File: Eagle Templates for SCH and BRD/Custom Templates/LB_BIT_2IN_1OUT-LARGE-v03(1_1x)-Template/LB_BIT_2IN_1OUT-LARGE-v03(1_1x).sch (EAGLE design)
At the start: 22 parts, among them U1 LV321SOT23-5, U2 LV321SOT23-5, U6 LV321SOT23-5

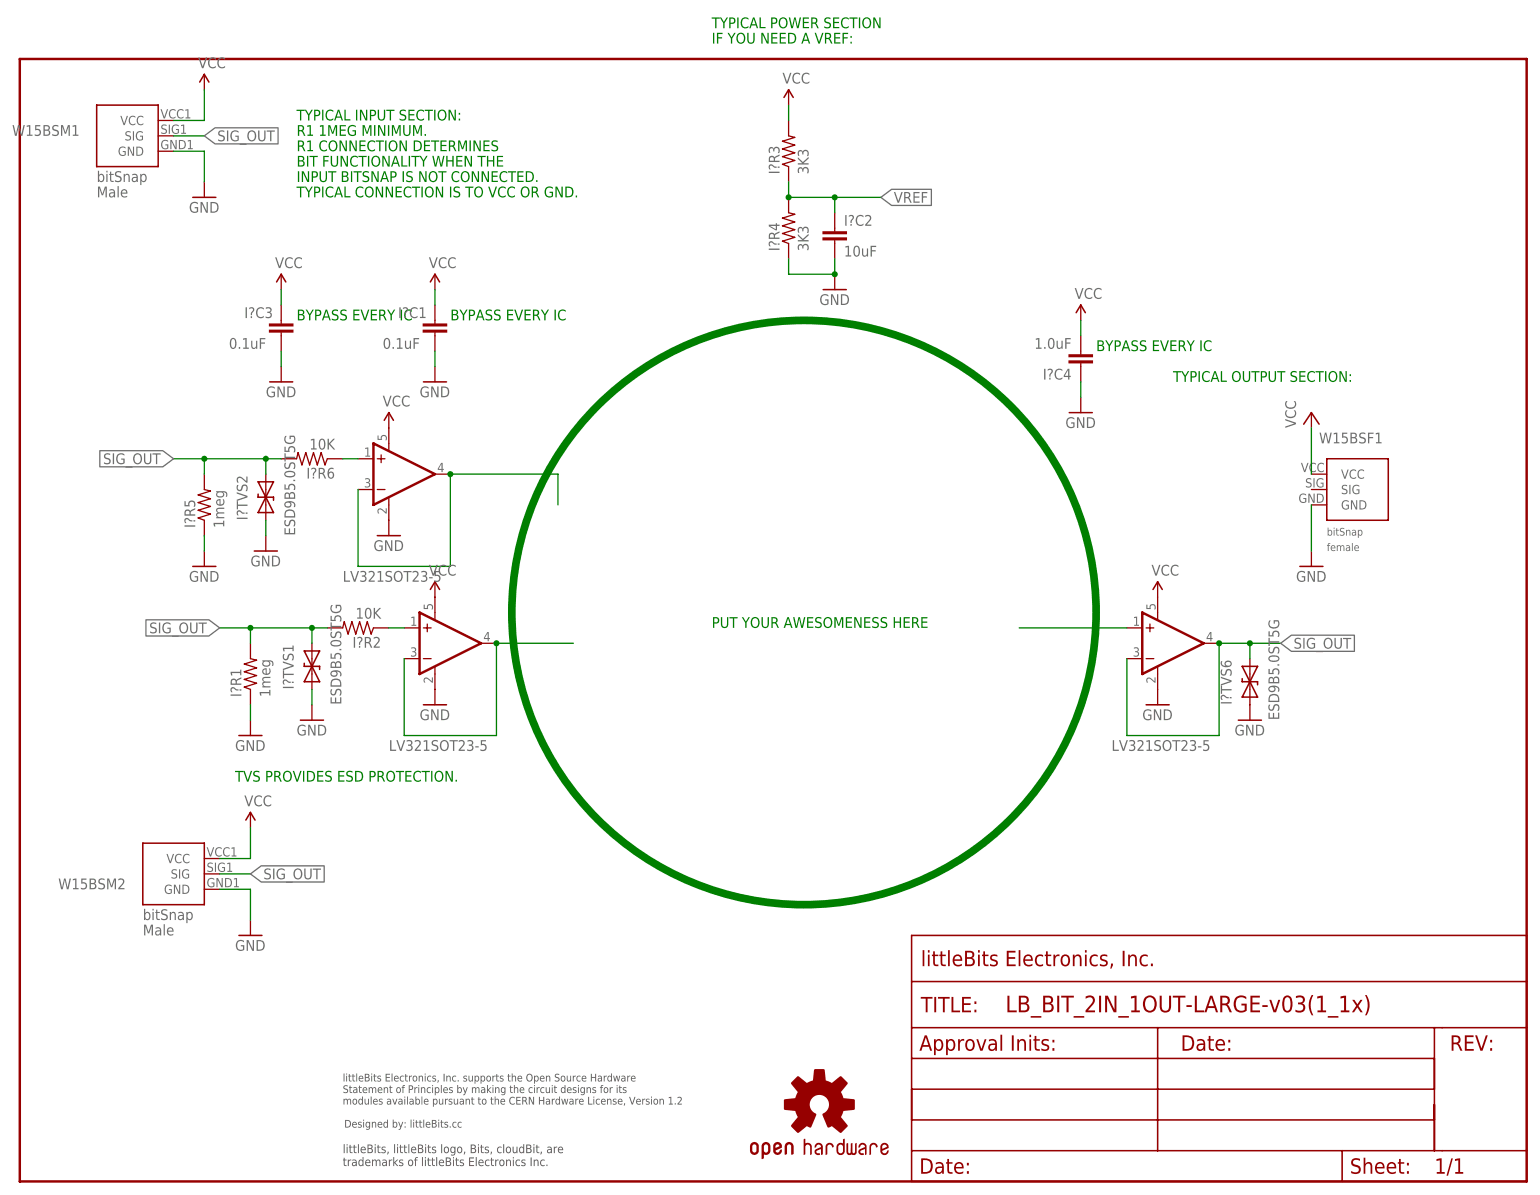
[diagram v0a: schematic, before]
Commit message: Updated templates
- Added ferrite beads
- Moved text and annotations off of Nets layer
- Minor layout changes
- Removed I/O/W prefix from reference designators
- Removed output stage components from output bits
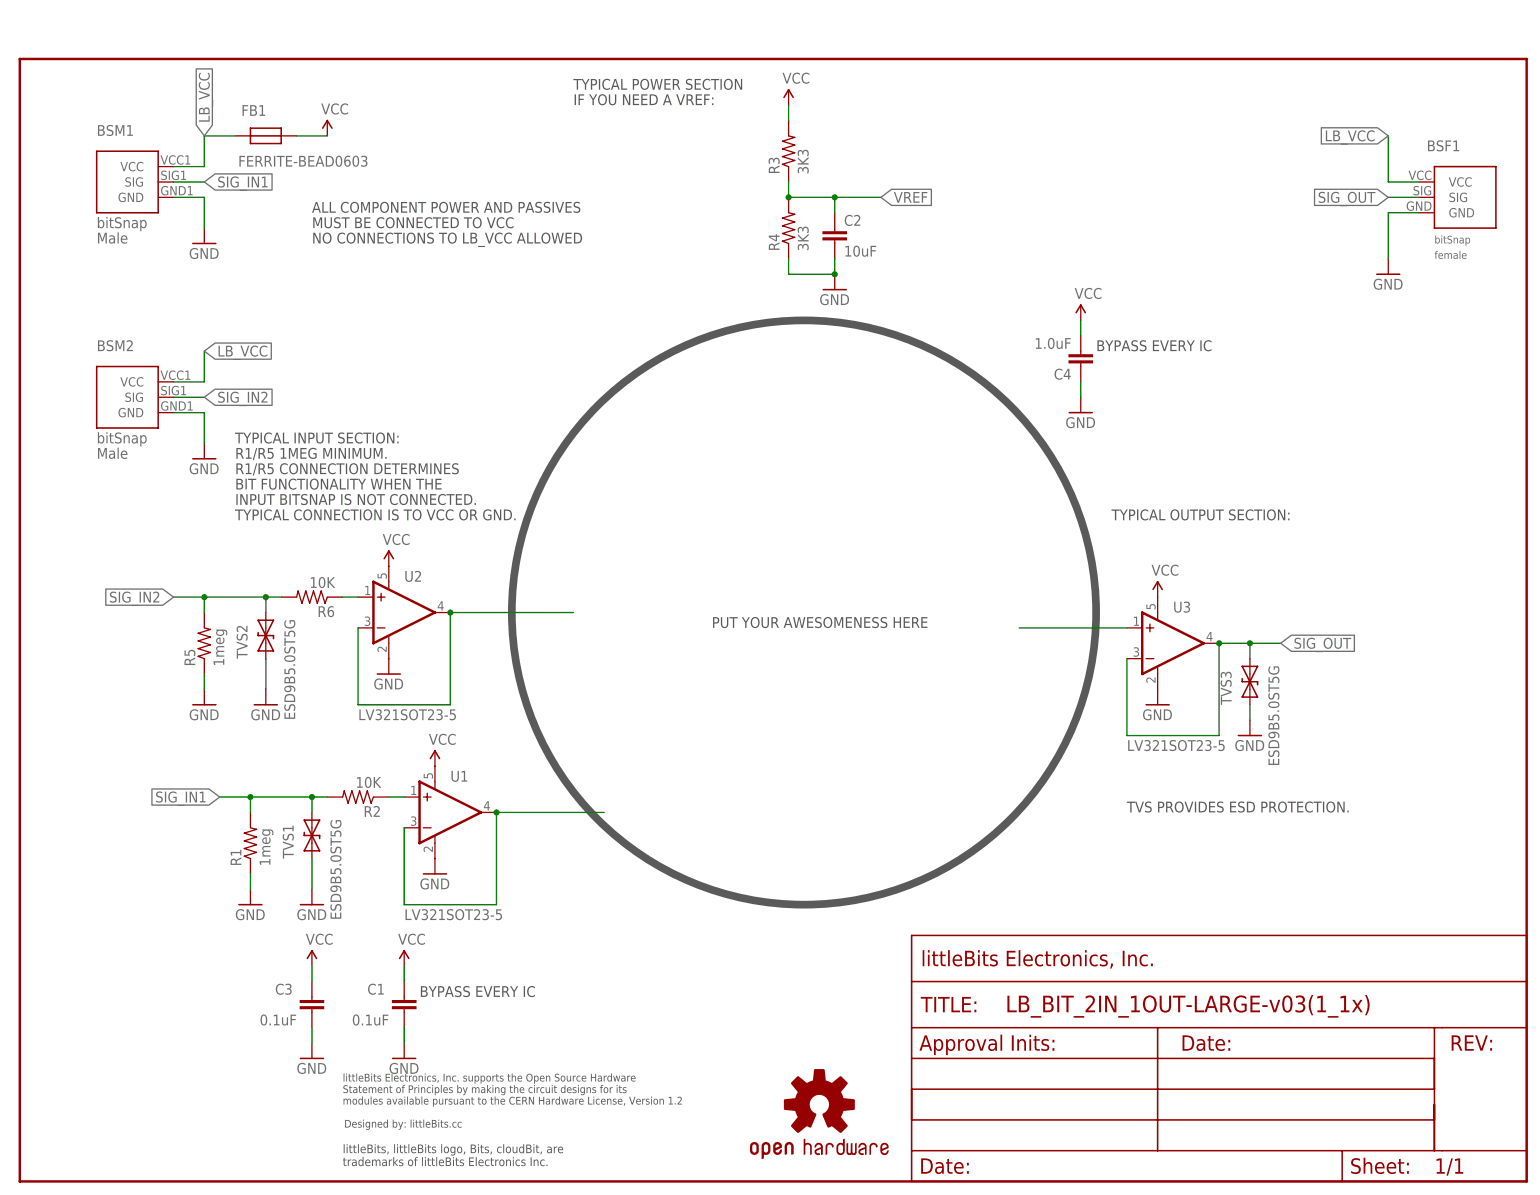
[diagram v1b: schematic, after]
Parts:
- removed I?C1, I?C3: 0.1uF, LITTLEBITS:CAPCAP-0603
- removed I?R1, I?R5: 1meg, LITTLEBITS:RESISTOR0603
- removed I?R2, I?R6: 10K, LITTLEBITS:RESISTOR0603
- removed I?TVS1, I?TVS2: ESD9B5.0ST5G, LITTLEBITS:DIODE-TVSSOD-923
- removed W15BSF1: BITSNAP_V03_FEMALE, bitSnap:BITSNAP_V03_FEMALE
- removed W15BSM1, W15BSM2: BITSNAP_V03_MALE, bitSnap:BITSNAP_V03_MALE
- added BSF1: BITSNAP_V03_FEMALE, bitSnap:BITSNAP_V03_FEMALE
- added BSM1, BSM2: BITSNAP_V03_MALE, bitSnap:BITSNAP_V03_MALE
- added C1, C3: 0.1uF, LITTLEBITS:CAPCAP-0603
- added FB1: FERRITE-BEAD0603, LITTLEBITS:FERRITE-BEAD0603
- added R1, R5: 1meg, LITTLEBITS:RESISTOR0603
- added R2, R6: 10K, LITTLEBITS:RESISTOR0603
- added TVS1, TVS2: ESD9B5.0ST5G, LITTLEBITS:DIODE-TVSSOD-923
- renumbered I?C2 to C2, I?C4 to C4, I?R3 to R3, I?R4 to R4, I?TVS6 to TVS3, U6 to U3
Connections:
- new net LB_VCC: BSF1.VCC, BSM1.VCC, BSM2.VCC, FB1.P$2
- new net SIG_IN1: BSM1.SIG, R1.2, R2.2, TVS1.C
- new net SIG_IN2: BSM2.SIG, R5.2, R6.2, TVS2.C
- net GND: now also BSF1.GND, BSM1.GND, BSM2.GND, C1.2, C3.2, R1.1, R5.1, TVS1.A, TVS2.A; no longer I?C1.2, I?C3.2, I?R1.1, I?R5.1, I?TVS1.A, I?TVS2.A, W15BSF1.GND, W15BSM1.GND, W15BSM2.GND
- net N$2: now also R6.1; no longer I?R6.1
- net N$4: now also R2.1; no longer I?R2.1
- net SIG_OUT: now also BSF1.SIG; no longer I?R1.2, I?R2.2, I?R5.2, I?R6.2, I?TVS1.C, I?TVS2.C, W15BSM1.SIG, W15BSM2.SIG
- net VCC: now also C1.1, C3.1, FB1.P$1; no longer I?C1.1, I?C3.1, W15BSF1.VCC, W15BSM1.VCC, W15BSM2.VCC
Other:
- note added: "ALL COMPONENT POWER AND PASSIVES"
- note added: "MUST BE CONNECTED TO VCC"
- note added: "NO CONNECTIONS TO LB_VCC ALLOWED"
- note added: "R1/R5 1MEG MINIMUM."
- note added: "R1/R5 CONNECTION DETERMINES"
- note removed: "R1 1MEG MINIMUM."
- note removed: "R1 CONNECTION DETERMINES"
